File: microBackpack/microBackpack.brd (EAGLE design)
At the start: 160 x 100 mm, 9 parts, among them IC1 LM324D, U1 ATMEGA328P_TQFP, U2 5VREG-HS, U3 CP2102N-QFN24

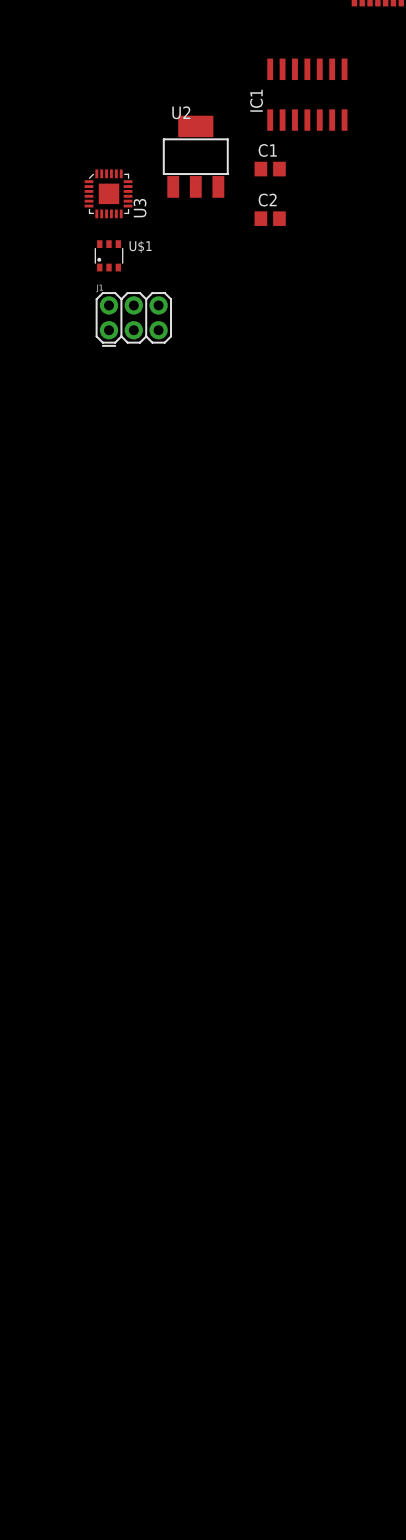
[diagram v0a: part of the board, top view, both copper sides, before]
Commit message: Added more components
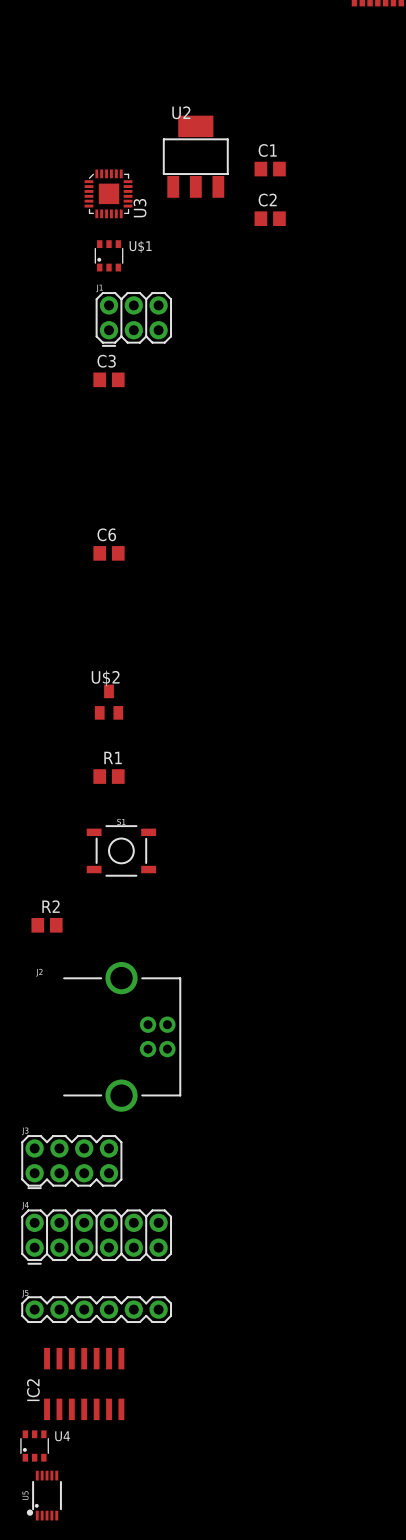
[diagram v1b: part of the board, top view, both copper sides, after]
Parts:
- removed IC1: LM324D, linear:SO14
- added C3: 1uF, rcl:C0805
- added C6: 10nF, rcl:C0805
- added IC2: LM324D, linear:SO14
- added J2: USB_B_PTH, SparkFun-Connectors:USB-B-PTH
- added J3: (no value), SparkFun-Connectors:2X4
- added J4: 2X6 FEMALE, SparkFun-Connectors:2X6
- added J5: (no value), SparkFun-Connectors:1X06
- added R1, R2: 1k, rcl:R0805
- added S1: MOMENTARY-SWITCH-SPST-SMD-5.2-REDUNDANT, SparkFun-Switches:TACTILE_SWITCH_SMD_5.2MM
- added U$2: LM4040-V-REF, microBackpackLib:SOT23
- added U4: TVS_DIODE_4PK, microBackpackLib:SOT457
- added U5: MCP4728, microBackpackLib:MSOP10
- C1, C2: value (none) -> 22pF
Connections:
- new net A2: J3.5
- new net A3: J3.7
- new net AD0+: J3.1
- new net AD0-: J3.2
- new net AD1+: J3.3
- new net AD1-: J3.4
- new net ADC0: U1.23
- new net ADC1: U1.24
- new net ADC2: U1.25
- new net ADC3: U1.26
- new net ADC6: U1.19
- new net ADC7: U1.22
- new net DIO0: J4.1, U1.32
- new net DIO1: J4.2, U1.1
- new net DIO2: J4.3, U1.2
- new net DIO3: J4.4, U1.9
- new net DIO4: J4.5, U1.10
- new net DIO5: J4.6, U1.11
- new net DIO6: J4.7, U1.12
- new net DIO7: J4.8, U1.13
- new net I_OUT: J5.5
- new net I_SET: J5.3
- new net LDAC: U1.14, U5.4
- new net MCU2USB: U1.31
- new net N$3: R1.1, U$2.1, U1.20
- new net N$4: J2.GND, J2.SHLD1, J2.SHLD2, U$1.2, U$1.5, U3.2
- new net N$5: J2.VBUS, U3.8
- new net N$7: J2.D-, U3.4
- new net N$8: J2.D+, U3.3
- new net SCL: U1.28, U5.2
- new net SDA: U1.27, U5.3
- new net USB2MCU: U1.30
- new net V_OUT: J5.4
- new net V_SET: J5.2
- net 12V: now also J5.1
- net GND: now also C3.2, C6.2, J3.6, J3.8, J4.12, J5.6, S1.1, S1.2, U$2.2, U1.21, U5.10
- net MISO: now also U1.16
- net MOSI: now also U1.15
- net RESET: now also R2.1, S1.3, S1.4, U1.29
- net SCK: now also U1.17
- net V+: now also IC2.4; no longer IC1.4
- net V-: now also IC2.11; no longer IC1.11
- net VCC: now also C3.1, C6.1, R1.2, R2.2, U1.18, U1.4, U1.6, U5.1

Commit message: Added analog circuitry. Most of schem is done. Still must do optoisolation and DIO protection
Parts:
- added C4, C8: 10nF, rcl:C0805
- added C5, C7, C9: 1uF, rcl:C0805
- added IC1: LM324D, linear:SO14
- added R10, R12, R13, R16, R17, R20, R24, R25, R27, R28, R6, R8: 10k, rcl:R0805
- added R11, R14, R15, R18, R19, R26, R5, R7: 30.1k, rcl:R0805
- added R21, R22: 1k, rcl:R0805
- added R23, R9: 15k, rcl:R0805
- added R3, R4: 4.7k, rcl:R0805
- added U6: 78L09F, linear:SOT89
- moved IC2 181.6 mm to (-48.3, -320.0)
- renumbered U$2 to D1
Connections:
- removed net V+: IC2.4
- removed net V-: IC2.11
- new net 2V_REF: R16.1, R20.1, R21.1, R22.2
- new net 4V_REF: C8.1, D1.1, R1.1, R21.2, U1.20
- new net 9V: C4.1, C5.1, IC1.4, U6.1
- new net DAC_A: IC2.3, U5.6
- new net DAC_B: R26.2, U5.7
- new net DAC_C: IC1.12, U5.8
- new net DAC_D: U5.9
- new net FGEN: IC1.14, R24.1
- new net N$10: IC1.5, R14.2, R16.2
- new net N$11: IC2.2, R27.2, R28.1
- new net N$14: IC1.9, R17.1, R19.2
- new net N$15: IC1.10, R18.2, R20.2
- new net N$6: IC1.2, R11.2, R12.1
- new net N$9: IC1.6, R13.1, R15.2
- net 12V: now also C7.1, C9.1, IC2.4, U6.3
- net A2: now also R5.2
- net A3: now also R7.2
- net AD0+: now also R14.1
- net AD0-: now also R15.1
- net AD1+: now also R18.1
- net AD1-: now also R19.1
- net ADC0: now also IC1.7, R13.2
- net ADC1: now also IC1.8, R17.2
- net ADC2: now also R10.2, R9.1
- net ADC3: now also IC1.1, R11.1
- net ADC6: now also R5.1, R6.2
- net ADC7: now also R7.1, R8.2
- net GND: now also C4.2, C5.2, C7.2, C8.2, C9.2, IC1.11, IC2.11, R10.1, R12.2, R22.1, R23.2, R25.1, R28.2, R6.1, R8.1, U6.2, U6.2@1
- net I_OUT: now also IC1.3
- net I_SET: now also R25.2, R26.1
- net N$3: now also IC1.13, R23.1, R24.2; no longer D1.1, R1.1, U1.20
- net SCL: now also R4.1
- net SDA: now also R3.1
- net VCC: now also R3.2, R4.2
- net V_OUT: now also R9.2
- net V_SET: now also IC2.1, R27.1

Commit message: Began board layout. Defined dimensions.
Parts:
- removed U$1: TVS_DIODE_4PK, microBackpackLib:SOT457
- added FGEN, FGEN_GND: TPPAD1-20Y, testpad:P1-20Y
- added H1, H2, H3, H4, H5: MOUNT-HOLE2.8, holes:2,8
- added U7: TVS_DIODE_4PK, microBackpackLib:SOT457
- moved U6 366.4 mm to (53.1, 67.8)
- moved R23 317.8 mm to (100.3, -48.8)
- moved C9 317.8 mm to (100.3, -61.5)
- moved R24 317.8 mm to (100.3, -55.1)
- moved R25 317.8 mm to (100.3, -67.8)
- moved IC2 312.0 mm to (29.2, -17.8)
- moved R26 296.1 mm to (60.7, -79.2)
- moved R27 296.1 mm to (60.7, -85.6)
- moved R28 296.1 mm to (60.7, -91.9)
- moved C4 240.2 mm to (49.0, -74.2)
- moved C5 240.2 mm to (49.0, -80.5)
- moved C7 240.2 mm to (49.0, -86.9)
- moved R22 240.2 mm to (49.0, -56.4)
- moved C8 240.2 mm to (49.0, -93.2)
- moved J4 236.2 mm to (115.6, 40.6), turned to 270 degrees
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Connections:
- net FGEN: now also FGEN.TP
- net GND: now also FGEN_GND.TP
- net N$4: now also U7.2, U7.5; no longer U$1.2, U$1.5
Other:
- board size 160 x 100 mm -> 121.9 x 76.2 mm

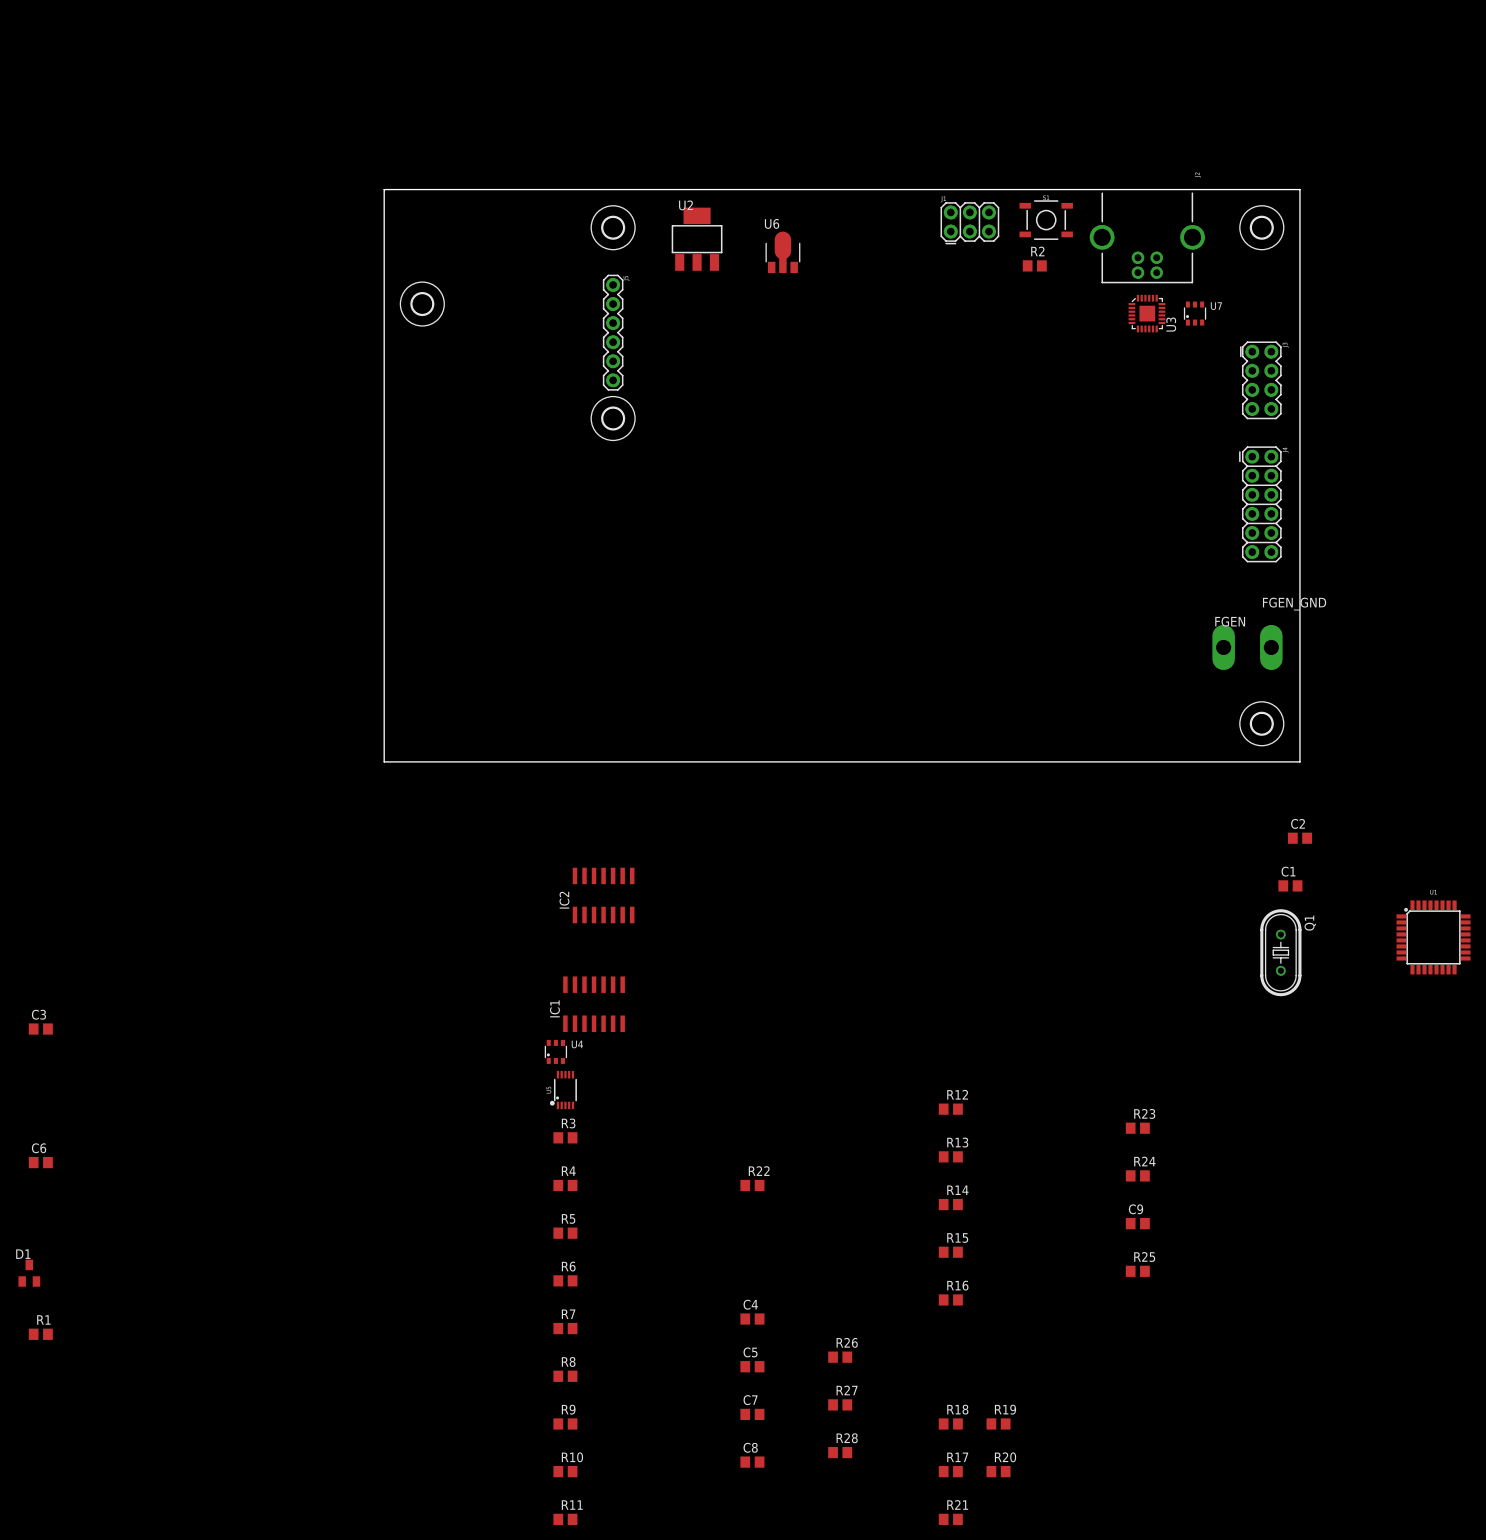
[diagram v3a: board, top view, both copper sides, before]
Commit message: Began op amp placement. Very rough
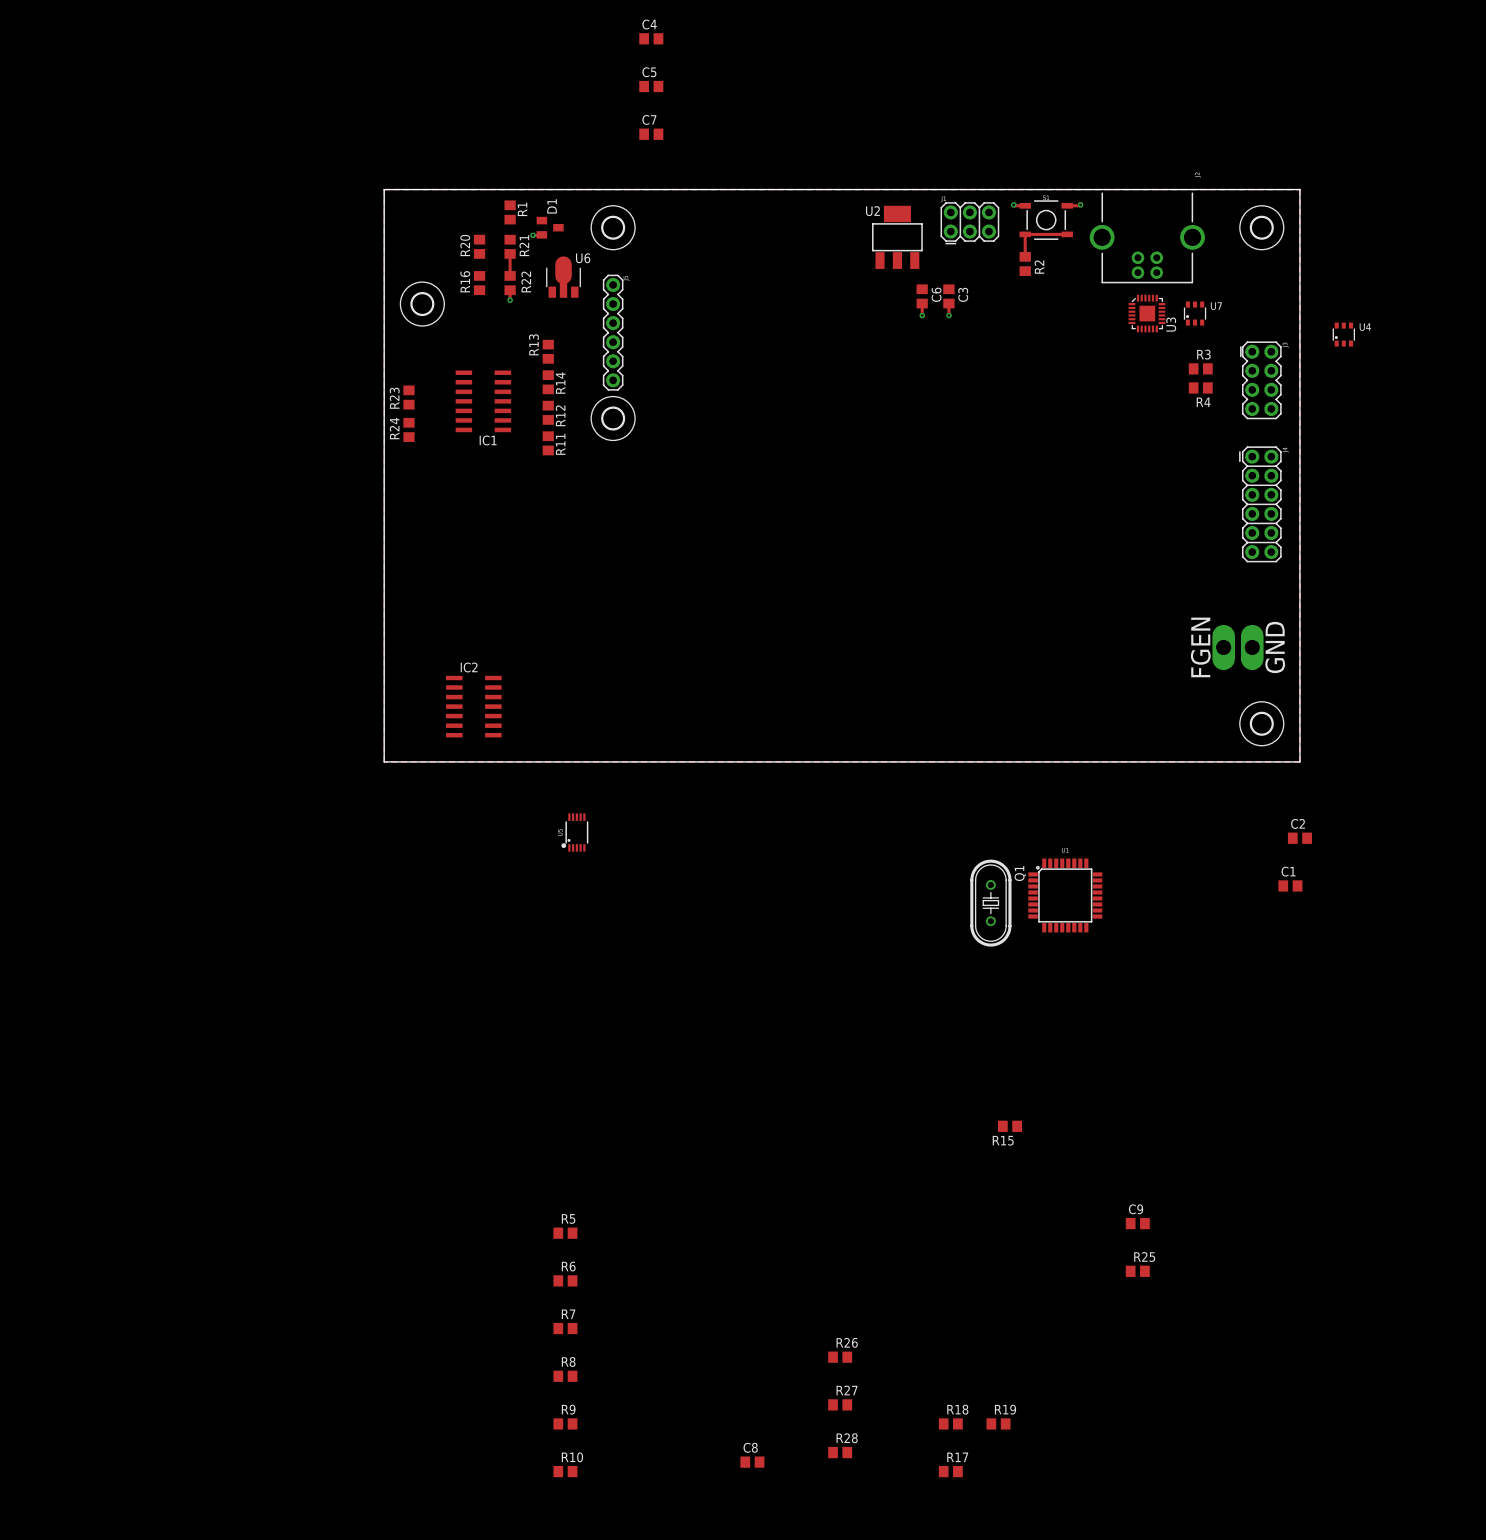
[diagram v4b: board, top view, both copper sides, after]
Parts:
- moved R21 179.3 mm to (16.8, 68.6), turned to 90 degrees
- moved R20 177.1 mm to (12.7, 68.6), turned to 90 degrees
- moved C4 171.0 mm to (35.6, 96.3)
- moved C5 171.0 mm to (35.6, 89.9)
- moved C7 171.0 mm to (35.6, 83.6)
- moved C6 164.5 mm to (71.6, 62.0), turned to 270 degrees
- moved R1 161.9 mm to (16.8, 73.2), turned to 90 degrees
- moved D1 155.5 mm to (22.1, 71.1), turned to 270 degrees
- moved C3 155.3 mm to (75.2, 62.0), turned to 270 degrees
- moved R16 149.2 mm to (12.7, 63.8), turned to 270 degrees
- moved R11 143.3 mm to (21.8, 42.4), turned to 90 degrees
- moved U4 141.9 mm to (127.8, 56.9)
- moved R24 138.8 mm to (3.30, 44.2), turned to 90 degrees
- moved R23 137.4 mm to (3.30, 48.5), turned to 90 degrees
- moved R4 135.7 mm to (108.7, 49.8)
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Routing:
- net GND: track 0.00 -> 9.14 mm, vias 0 -> 6
- net RESET: track 0.00 -> 8.58 mm
- net 2V_REF: track 0.00 -> 2.93 mm
- added copper zone on layer 16, net GND
- added copper zone on layer 1, net VCC
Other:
- board text added: "GND"
